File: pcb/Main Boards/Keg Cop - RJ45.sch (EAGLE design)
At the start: 14 parts, among them X1 RJ45-8X, X2 RJ45-8X

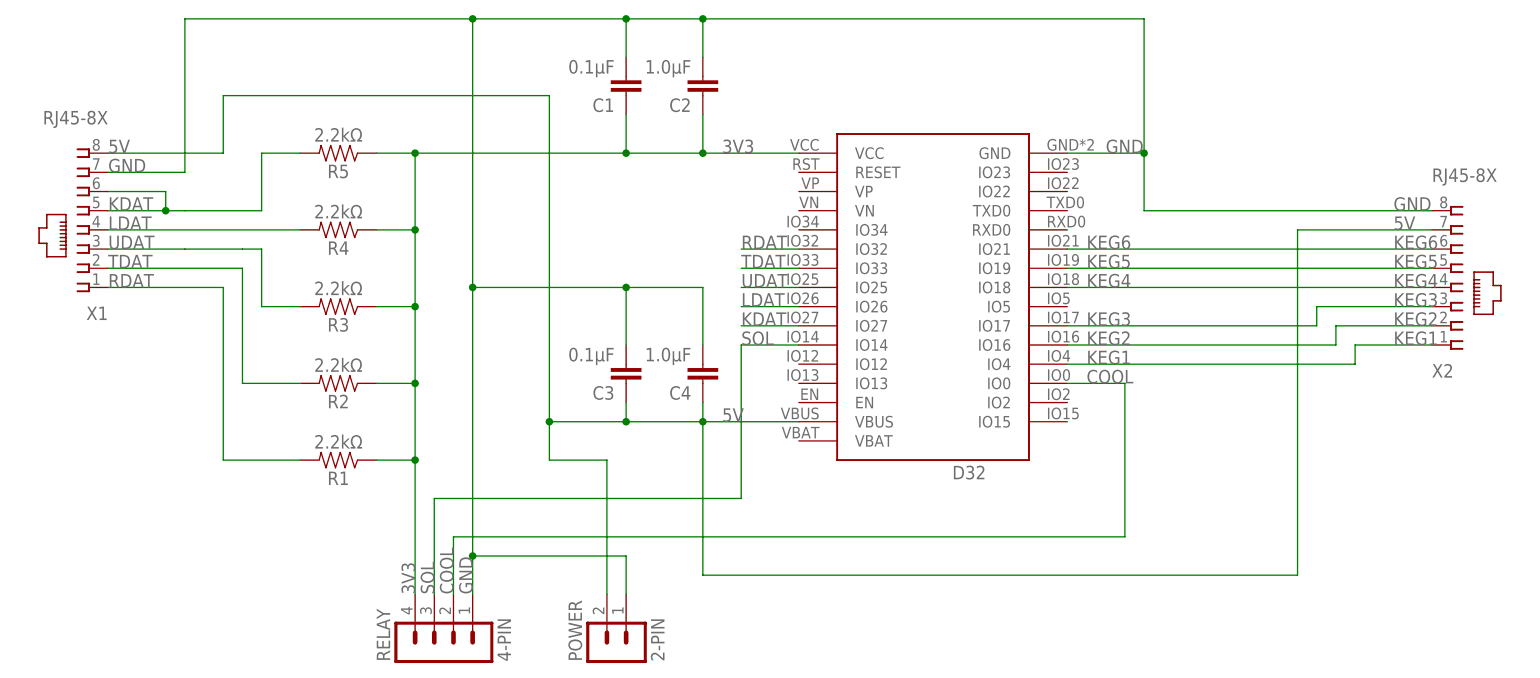
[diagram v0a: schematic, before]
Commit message: Swap pins, split dirs
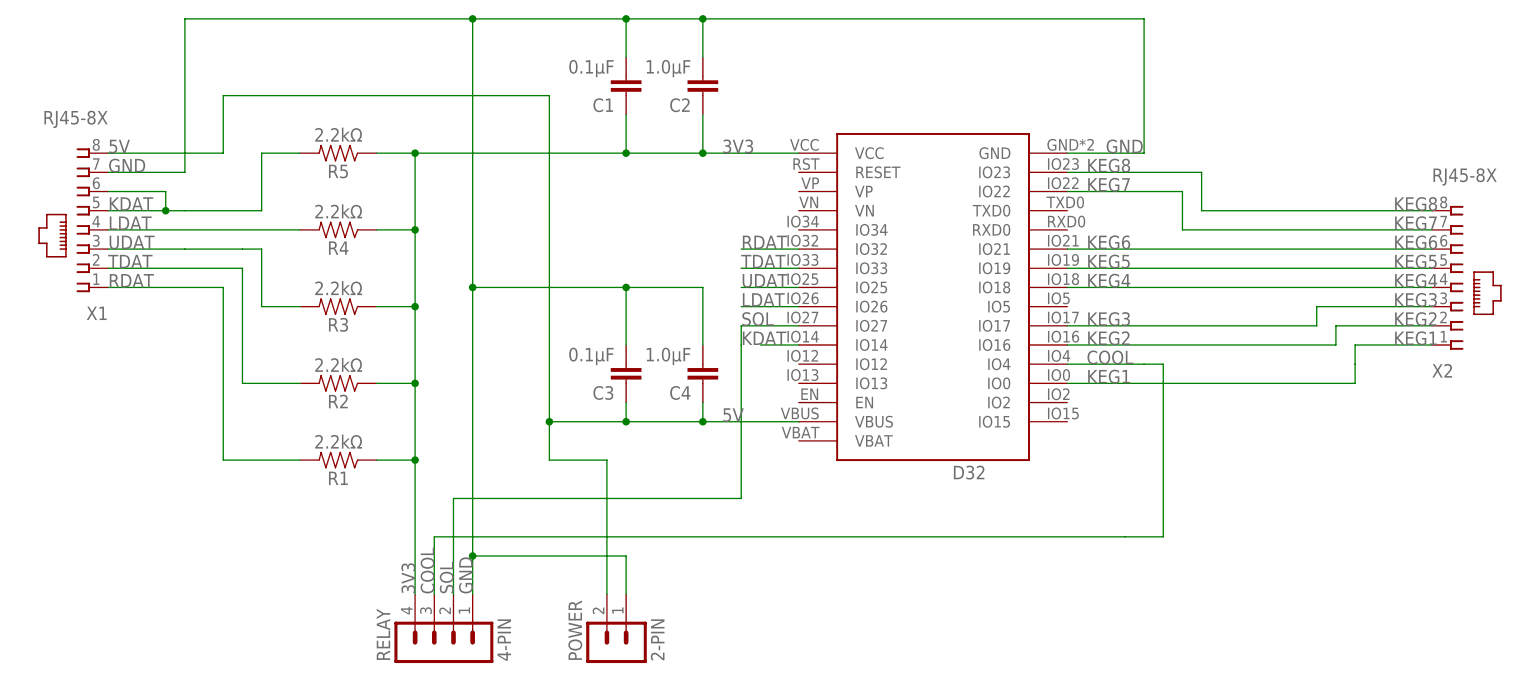
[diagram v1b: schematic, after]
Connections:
- new net KEG7: D32.IO22, X2.7
- new net KEG8: D32.IO23, X2.8
- net 5V: no longer X2.7
- net COOL: now also D32.IO4, RELAY.3; no longer D32.IO0, RELAY.2
- net GND: no longer X2.8
- net KDAT: now also D32.IO14; no longer D32.IO27
- net KEG1: now also D32.IO0; no longer D32.IO4
- net SOL: now also D32.IO27, RELAY.2; no longer D32.IO14, RELAY.3
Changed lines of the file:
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@@
 <pinref part="X1" gate="G$1" pin="8"/>
 <wire x1="-48.26" y1="71.12" x2="-63.5" y2="71.12" width="0.1524" layer="91"/>
-<wire x1="15.24" y1="35.56" x2="15.24" y2="15.24" width="0.1524" layer="91"/>
-<wire x1="15.24" y1="15.24" x2="93.98" y2="15.24" width="0.1524" layer="91"/>
-<wire x1="93.98" y1="15.24" x2="93.98" y2="60.96" width="0.1524" layer="91"/>
-<pinref part="X2" gate="G$1" pin="7"/>
-<wire x1="111.76" y1="60.96" x2="93.98" y2="60.96" width="0.1524" layer="91"/>
-<label x="106.68" y="60.96" size="1.778" layer="95"/>
 </segment>
 </net>
@@
 <pinref part="X1" gate="G$1" pin="7"/>
 <wire x1="-53.34" y1="68.58" x2="-63.5" y2="68.58" width="0.1524" layer="91"/>
-<pinref part="X2" gate="G$1" pin="8"/>
-<wire x1="73.66" y1="71.12" x2="73.66" y2="63.5" width="0.1524" layer="91"/>
-<wire x1="73.66" y1="63.5" x2="111.76" y2="63.5" width="0.1524" layer="91"/>
-<junction x="73.66" y="71.12"/>
-<label x="106.68" y="63.5" size="1.778" layer="95"/>
 </segment>
 </net>
 <net name="SOL" class="0">
 <segment>
+<wire x1="20.32" y1="45.72" x2="20.32" y2="25.4" width="0.1524" layer="91"/>
+<wire x1="20.32" y1="25.4" x2="-17.78" y2="25.4" width="0.1524" layer="91"/>
+<pinref part="RELAY" gate="1" pin="2"/>
+<wire x1="-17.78" y1="25.4" x2="-17.78" y2="12.7" width="0.1524" layer="91"/>
+<label x="-17.78" y="12.7" size="1.778" layer="95" rot="R90"/>
+<wire x1="20.32" y1="45.72" x2="20.32" y2="48.26" width="0.1524" layer="91"/>
+<pinref part="D32" gate="G$1" pin="IO27"/>
+<wire x1="20.32" y1="48.26" x2="27.94" y2="48.26" width="0.1524" layer="91"/>
+<label x="20.32" y="48.26" size="1.778" layer="95"/>
+</segment>
+</net>
+<net name="COOL" class="0">
+<segment>
+<wire x1="71.12" y1="20.32" x2="-20.32" y2="20.32" width="0.1524" layer="91"/>
 <pinref part="RELAY" gate="1" pin="3"/>
-<wire x1="-20.32" y1="12.7" x2="-20.32" y2="25.4" width="0.1524" layer="91"/>
+<wire x1="-20.32" y1="20.32" x2="-20.32" y2="12.7" width="0.1524" layer="91"/>
 <label x="-20.32" y="12.7" size="1.778" layer="95" rot="R90"/>
-<pinref part="D32" gate="G$1" pin="IO14"/>
-<wire x1="27.94" y1="45.72" x2="20.32" y2="45.72" width="0.1524" layer="91"/>
-<wire x1="20.32" y1="45.72" x2="20.32" y2="25.4" width="0.1524" layer="91"/>
-<wire x1="20.32" y1="25.4" x2="-20.32" y2="25.4" width="0.1524" layer="91"/>
-<label x="20.32" y="45.72" size="1.778" layer="95"/>
-</segment>
-</net>
-<net name="COOL" class="0">
-<segment>
-<pinref part="RELAY" gate="1" pin="2"/>
-<label x="-17.78" y="12.7" size="1.778" layer="95" rot="R90"/>
-<pinref part="D32" gate="G$1" pin="IO0"/>
-<wire x1="63.5" y1="40.64" x2="71.12" y2="40.64" width="0.1524" layer="91"/>
-<wire x1="71.12" y1="40.64" x2="71.12" y2="20.32" width="0.1524" layer="91"/>
-<wire x1="71.12" y1="20.32" x2="-17.78" y2="20.32" width="0.1524" layer="91"/>
-<wire x1="-17.78" y1="20.32" x2="-17.78" y2="12.7" width="0.1524" layer="91"/>
-<label x="66.04" y="40.64" size="1.778" layer="95"/>
+<wire x1="71.12" y1="20.32" x2="76.2" y2="20.32" width="0.1524" layer="91"/>
+<wire x1="76.2" y1="20.32" x2="76.2" y2="43.18" width="0.1524" layer="91"/>
+<wire x1="76.2" y1="43.18" x2="73.66" y2="43.18" width="0.1524" layer="91"/>
+<pinref part="D32" gate="G$1" pin="IO4"/>
+<wire x1="73.66" y1="43.18" x2="63.5" y2="43.18" width="0.1524" layer="91"/>
+<label x="66.04" y="43.18" size="1.778" layer="95"/>
 </segment>
 </net>
@@
 </segment>
 <segment>
-<pinref part="D32" gate="G$1" pin="IO27"/>
-<wire x1="27.94" y1="48.26" x2="20.32" y2="48.26" width="0.1524" layer="91"/>
-<label x="20.32" y="48.26" size="1.778" layer="95"/>
+<pinref part="D32" gate="G$1" pin="IO14"/>
+<wire x1="27.94" y1="45.72" x2="22.86" y2="45.72" width="0.1524" layer="91"/>
+<label x="20.32" y="45.72" size="1.778" layer="95"/>
 </segment>
 </net>
@@
 </segment>
 </net>
+<net name="KEG7" class="0">
+<segment>
+<pinref part="D32" gate="G$1" pin="IO22"/>
+<label x="66.04" y="66.04" size="1.778" layer="95"/>
+<wire x1="63.5" y1="66.04" x2="78.74" y2="66.04" width="0.1524" layer="91"/>
+<wire x1="78.74" y1="66.04" x2="78.74" y2="60.96" width="0.1524" layer="91"/>
+<label x="106.68" y="60.96" size="1.778" layer="95"/>
+<pinref part="X2" gate="G$1" pin="7"/>
+<wire x1="78.74" y1="60.96" x2="111.76" y2="60.96" width="0.1524" layer="91"/>
+</segment>
+</net>
+<net name="KEG8" class="0">
+<segment>
+<pinref part="D32" gate="G$1" pin="IO23"/>
+<label x="66.04" y="68.58" size="1.778" layer="95"/>
+<wire x1="63.5" y1="68.58" x2="81.28" y2="68.58" width="0.1524" layer="91"/>
+<wire x1="81.28" y1="68.58" x2="81.28" y2="63.5" width="0.1524" layer="91"/>
+<label x="106.68" y="63.5" size="1.778" layer="95"/>
+<pinref part="X2" gate="G$1" pin="8"/>
+<wire x1="81.28" y1="63.5" x2="111.76" y2="63.5" width="0.1524" layer="91"/>
+</segment>
+</net>
 <net name="KEG1" class="0">
 <segment>
-<pinref part="D32" gate="G$1" pin="IO4"/>
-<label x="66.04" y="43.18" size="1.778" layer="95"/>
-<wire x1="63.5" y1="43.18" x2="101.6" y2="43.18" width="0.1524" layer="91"/>
 <wire x1="101.6" y1="43.18" x2="101.6" y2="45.72" width="0.1524" layer="91"/>
 <wire x1="101.6" y1="45.72" x2="111.76" y2="45.72" width="0.1524" layer="91"/>
 <label x="106.68" y="45.72" size="1.778" layer="95"/>
 <pinref part="X2" gate="G$1" pin="1"/>
-</segment>
-</net>
+<pinref part="D32" gate="G$1" pin="IO0"/>
+<wire x1="63.5" y1="40.64" x2="101.6" y2="40.64" width="0.1524" layer="91"/>
+<wire x1="101.6" y1="40.64" x2="101.6" y2="43.18" width="0.1524" layer="91"/>
+<label x="66.04" y="40.64" size="1.778" layer="95"/>
+</segment>
+</net>

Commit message: Renamed files
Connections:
- net COOL: now also D32.IO27, RELAY.2; no longer D32.IO4, RELAY.3
- net KEG2: now also D32.IO4; no longer D32.IO16
- net SOL: now also D32.IO16, RELAY.3; no longer D32.IO27, RELAY.2
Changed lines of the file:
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@@
-</segment>
-</net>
-<net name="SOL" class="0">
-<segment>
-<wire x1="20.32" y1="45.72" x2="20.32" y2="25.4" width="0.1524" layer="91"/>
-<wire x1="20.32" y1="25.4" x2="-17.78" y2="25.4" width="0.1524" layer="91"/>
-<pinref part="RELAY" gate="1" pin="2"/>
-<wire x1="-17.78" y1="25.4" x2="-17.78" y2="12.7" width="0.1524" layer="91"/>
-<label x="-17.78" y="12.7" size="1.778" layer="95" rot="R90"/>
-<wire x1="20.32" y1="45.72" x2="20.32" y2="48.26" width="0.1524" layer="91"/>
-<pinref part="D32" gate="G$1" pin="IO27"/>
-<wire x1="20.32" y1="48.26" x2="27.94" y2="48.26" width="0.1524" layer="91"/>
-<label x="20.32" y="48.26" size="1.778" layer="95"/>
-</segment>
-</net>
-<net name="COOL" class="0">
-<segment>
-<wire x1="71.12" y1="20.32" x2="-20.32" y2="20.32" width="0.1524" layer="91"/>
-<pinref part="RELAY" gate="1" pin="3"/>
-<wire x1="-20.32" y1="20.32" x2="-20.32" y2="12.7" width="0.1524" layer="91"/>
-<label x="-20.32" y="12.7" size="1.778" layer="95" rot="R90"/>
-<wire x1="71.12" y1="20.32" x2="76.2" y2="20.32" width="0.1524" layer="91"/>
-<wire x1="76.2" y1="20.32" x2="76.2" y2="43.18" width="0.1524" layer="91"/>
-<wire x1="76.2" y1="43.18" x2="73.66" y2="43.18" width="0.1524" layer="91"/>
-<pinref part="D32" gate="G$1" pin="IO4"/>
-<wire x1="73.66" y1="43.18" x2="63.5" y2="43.18" width="0.1524" layer="91"/>
-<label x="66.04" y="43.18" size="1.778" layer="95"/>
 </segment>
 </net>
@@
 <net name="KEG2" class="0">
 <segment>
-<pinref part="D32" gate="G$1" pin="IO16"/>
-<label x="66.04" y="45.72" size="1.778" layer="95"/>
-<wire x1="63.5" y1="45.72" x2="99.06" y2="45.72" width="0.1524" layer="91"/>
 <label x="106.68" y="48.26" size="1.778" layer="95"/>
 <pinref part="X2" gate="G$1" pin="2"/>
-<wire x1="99.06" y1="45.72" x2="99.06" y2="48.26" width="0.1524" layer="91"/>
 <wire x1="99.06" y1="48.26" x2="111.76" y2="48.26" width="0.1524" layer="91"/>
+<wire x1="99.06" y1="48.26" x2="99.06" y2="43.18" width="0.1524" layer="91"/>
+<pinref part="D32" gate="G$1" pin="IO4"/>
+<wire x1="99.06" y1="43.18" x2="63.5" y2="43.18" width="0.1524" layer="91"/>
+<label x="66.04" y="43.18" size="1.778" layer="95"/>
 </segment>
 </net>
@@
 </segment>
 </net>
+<net name="COOL" class="0">
+<segment>
+<pinref part="D32" gate="G$1" pin="IO27"/>
+<wire x1="27.94" y1="48.26" x2="17.78" y2="48.26" width="0.1524" layer="91"/>
+<wire x1="17.78" y1="48.26" x2="17.78" y2="43.18" width="0.1524" layer="91"/>
+<wire x1="17.78" y1="43.18" x2="22.86" y2="43.18" width="0.1524" layer="91"/>
+<wire x1="22.86" y1="43.18" x2="22.86" y2="33.02" width="0.1524" layer="91"/>
+<pinref part="RELAY" gate="1" pin="2"/>
+<wire x1="-17.78" y1="12.7" x2="-17.78" y2="33.02" width="0.1524" layer="91"/>
+<wire x1="-17.78" y1="33.02" x2="22.86" y2="33.02" width="0.1524" layer="91"/>
+<label x="20.32" y="48.26" size="1.778" layer="95"/>
+<label x="-17.78" y="12.7" size="1.778" layer="95" rot="R90"/>
+</segment>
+</net>
+<net name="SOL" class="0">
+<segment>
+<pinref part="D32" gate="G$1" pin="IO16"/>
+<wire x1="63.5" y1="45.72" x2="73.66" y2="45.72" width="0.1524" layer="91"/>
+<wire x1="73.66" y1="45.72" x2="73.66" y2="25.4" width="0.1524" layer="91"/>
+<pinref part="RELAY" gate="1" pin="3"/>
+<wire x1="73.66" y1="25.4" x2="-20.32" y2="25.4" width="0.1524" layer="91"/>
+<wire x1="-20.32" y1="25.4" x2="-20.32" y2="12.7" width="0.1524" layer="91"/>
+<label x="66.04" y="45.72" size="1.778" layer="95"/>
+<label x="-20.32" y="12.7" size="1.778" layer="95" rot="R90"/>
+</segment>
+</net>
